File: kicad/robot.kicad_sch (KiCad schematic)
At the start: 27 parts, among them J1 Accelerometer, M1 Motor_DC, M2 Motor_DC, M3 Motor_DC, M4 Motor_DC, Q1 NMOS, SW1 SW_Push_45deg, SW2 SW_Push_45deg, U1 LT1963AxQ-3.3, U2 ESP32-WROOM-32, U3 DRV8833PW, U4 DRV8833PW, U5 MAX1811

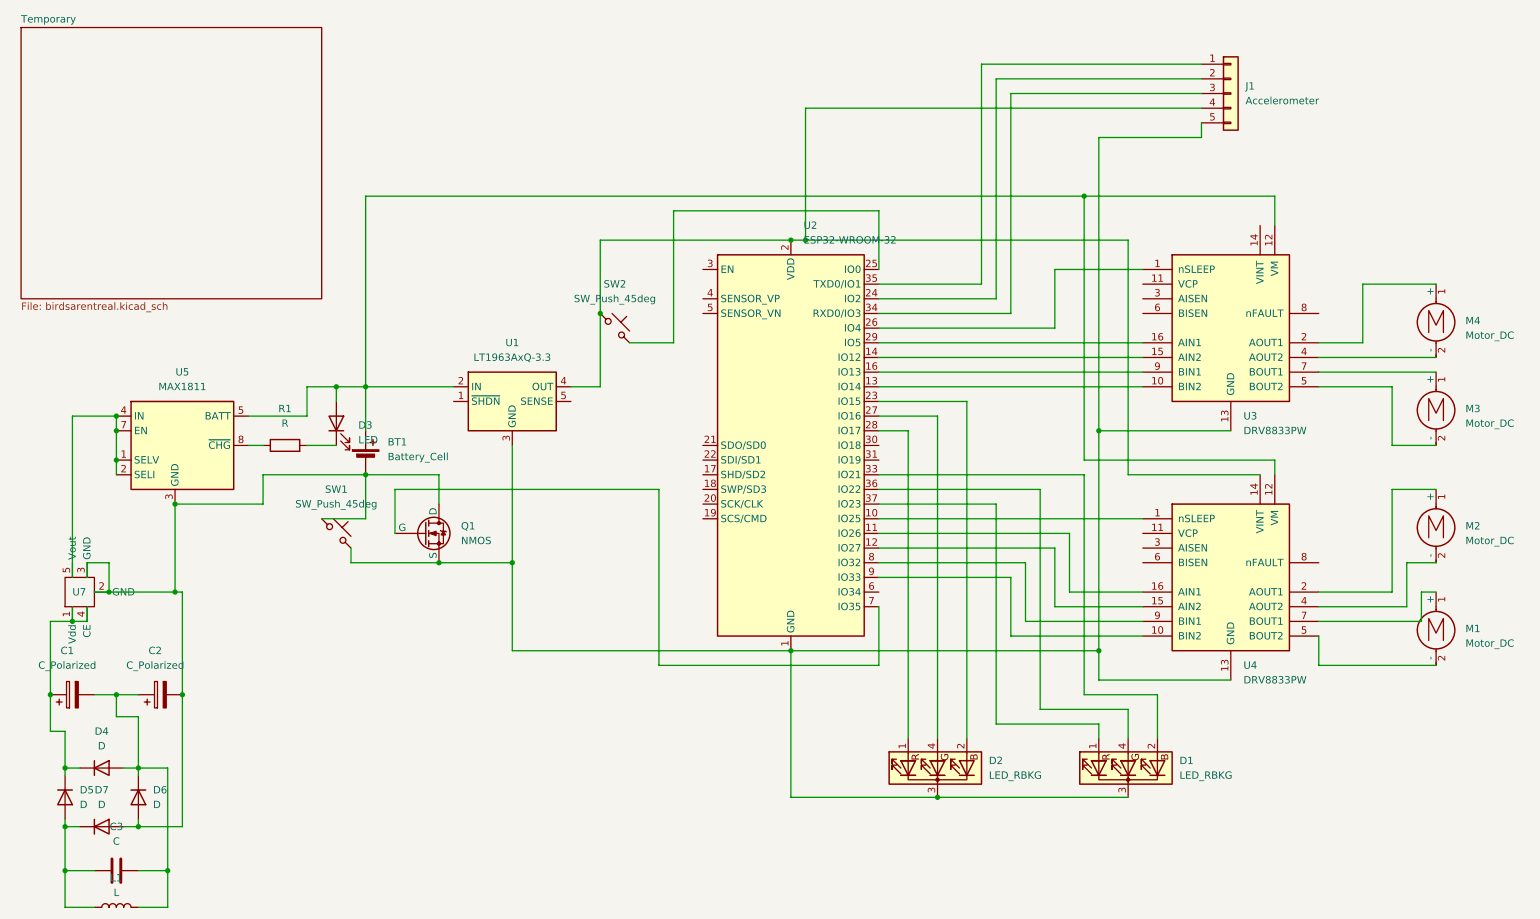
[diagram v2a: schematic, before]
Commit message: Fix footprints
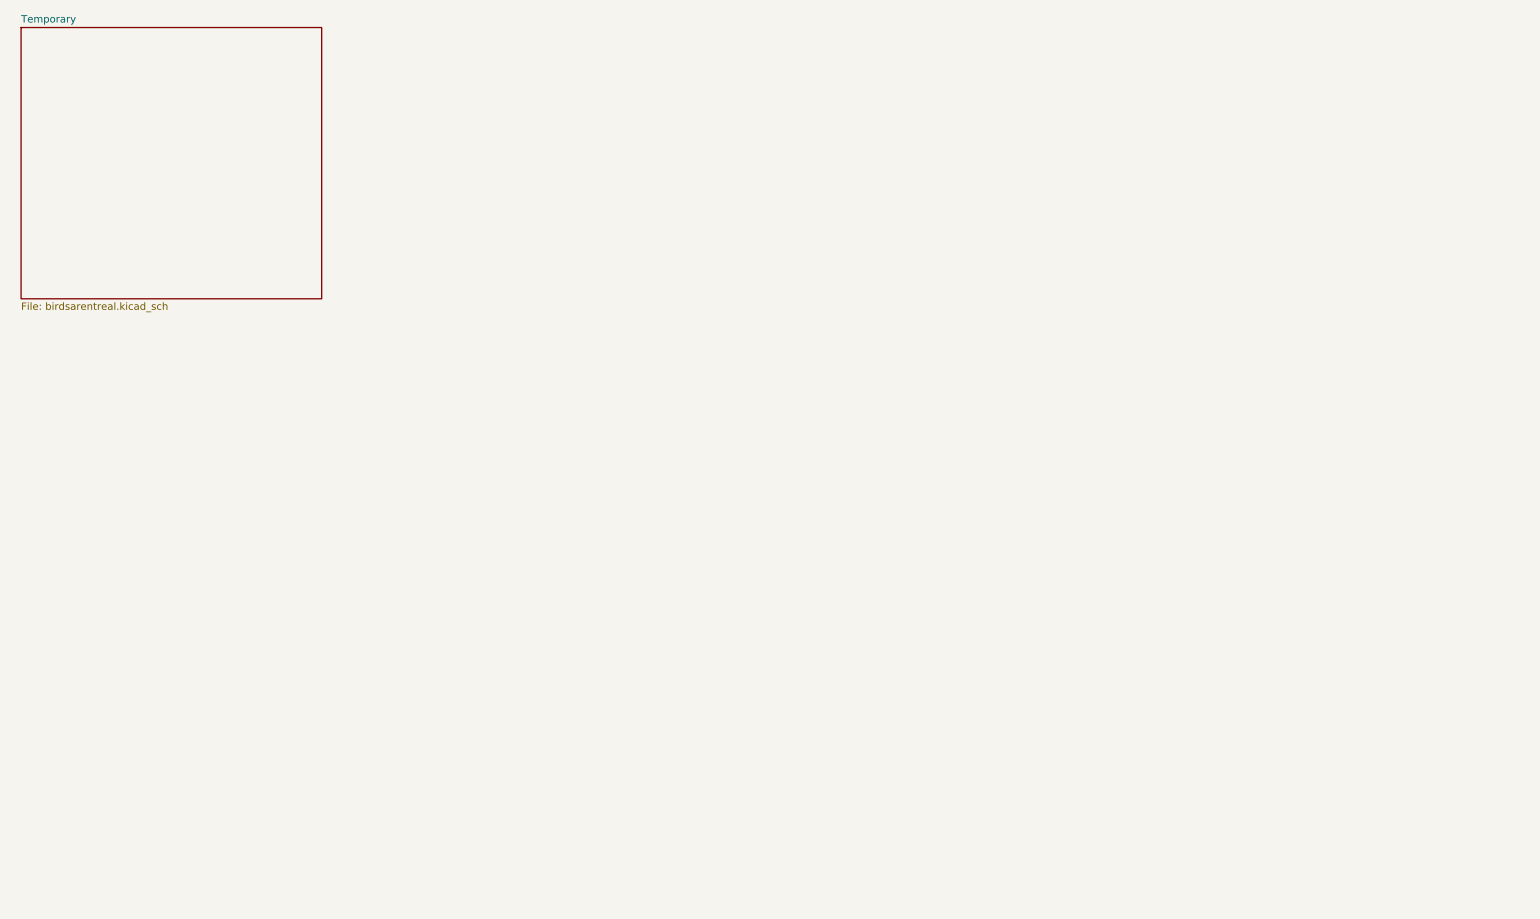
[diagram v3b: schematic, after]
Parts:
- removed BT1: Battery_Cell, symbol Device:Battery_Cell
- removed C1, C2: C_Polarized, symbol Device:C_Polarized
- removed C3: C, symbol Device:C
- removed D1: LED_RBKG, symbol Device:LED_RBKG
- removed D2: LED_RBKG, Connector_PinHeader_1.00mm:PinHeader_1x04_P1.00mm_Vertical, symbol Device:LED_RBKG
- removed D3: LED, symbol Device:LED
- removed D4, D5, D6, D7: D, symbol Device:D
- removed J1: Accelerometer, symbol Connector_Generic:Conn_01x05
- removed L1: L, symbol Device:L
- removed M1, M2, M3, M4: Motor_DC, symbol Motor:Motor_DC
- removed Q1: NMOS, symbol Simulation_SPICE:NMOS
- removed R1: R, symbol Device:R
- removed SW1, SW2: SW_Push_45deg, symbol Switch:SW_Push_45deg
- removed U1: LT1963AxQ-3.3, Package_TO_SOT_SMD:TO-263-5_TabPin3, symbol Regulator_Linear:LT1963AxQ-3.3
- removed U2: ESP32-WROOM-32, RF_Module:ESP32-WROOM-32, symbol RF_Module:ESP32-WROOM-32
- removed U3, U4: DRV8833PW, Package_SO:TSSOP-16_4.4x5mm_P0.65mm, symbol Driver_Motor:DRV8833PW
- removed U5: MAX1811, Package_SO:SOIC-8_3.9x4.9mm_P1.27mm, symbol Battery_Management:MAX1811
- removed U7: ~, Package_TO_SOT_SMD:SOT-89-5, symbol R1500H050B:R1500H050B
